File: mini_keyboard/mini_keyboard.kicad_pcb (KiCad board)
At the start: 2 copper layers, 4 parts, among them U1 MX1A-11NN, U2 MX1A-11NN, U3 MX1A-11NN, U4 MX1A-11NN

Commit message: adding more keys and looking at spacing
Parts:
- added U10: MX1A-11NN, pedrolib:CHERRY_MX1A-11NN_SWITCH, F.Cu at (54.0, 25.4)
- added U11: MX1A-11NN, pedrolib:CHERRY_MX1A-11NN_SWITCH, F.Cu at (73.0, 25.4)
- added U12: MX1A-11NN, pedrolib:CHERRY_MX1A-11NN_SWITCH, F.Cu at (92.1, 25.4)
- added U5: MX1A-11NN, pedrolib:CHERRY_MX1A-11NN_SWITCH, F.Cu at (44.5, 44.5)
- added U6: MX1A-11NN, pedrolib:CHERRY_MX1A-11NN_SWITCH, F.Cu at (63.5, 44.5)
- added U7: MX1A-11NN, pedrolib:CHERRY_MX1A-11NN_SWITCH, F.Cu at (82.5, 44.5)
- added U8: MX1A-11NN, pedrolib:CHERRY_MX1A-11NN_SWITCH, F.Cu at (101.6, 44.5)
- added U9: MX1A-11NN, pedrolib:CHERRY_MX1A-11NN_SWITCH, F.Cu at (34.9, 25.4)
- moved U4 59.1 mm to (108.0, 63.5)
- moved U1 50.0 mm to (50.8, 63.5)
- moved U3 43.6 mm to (88.9, 63.5)
- moved U2 39.6 mm to (69.8, 63.5)

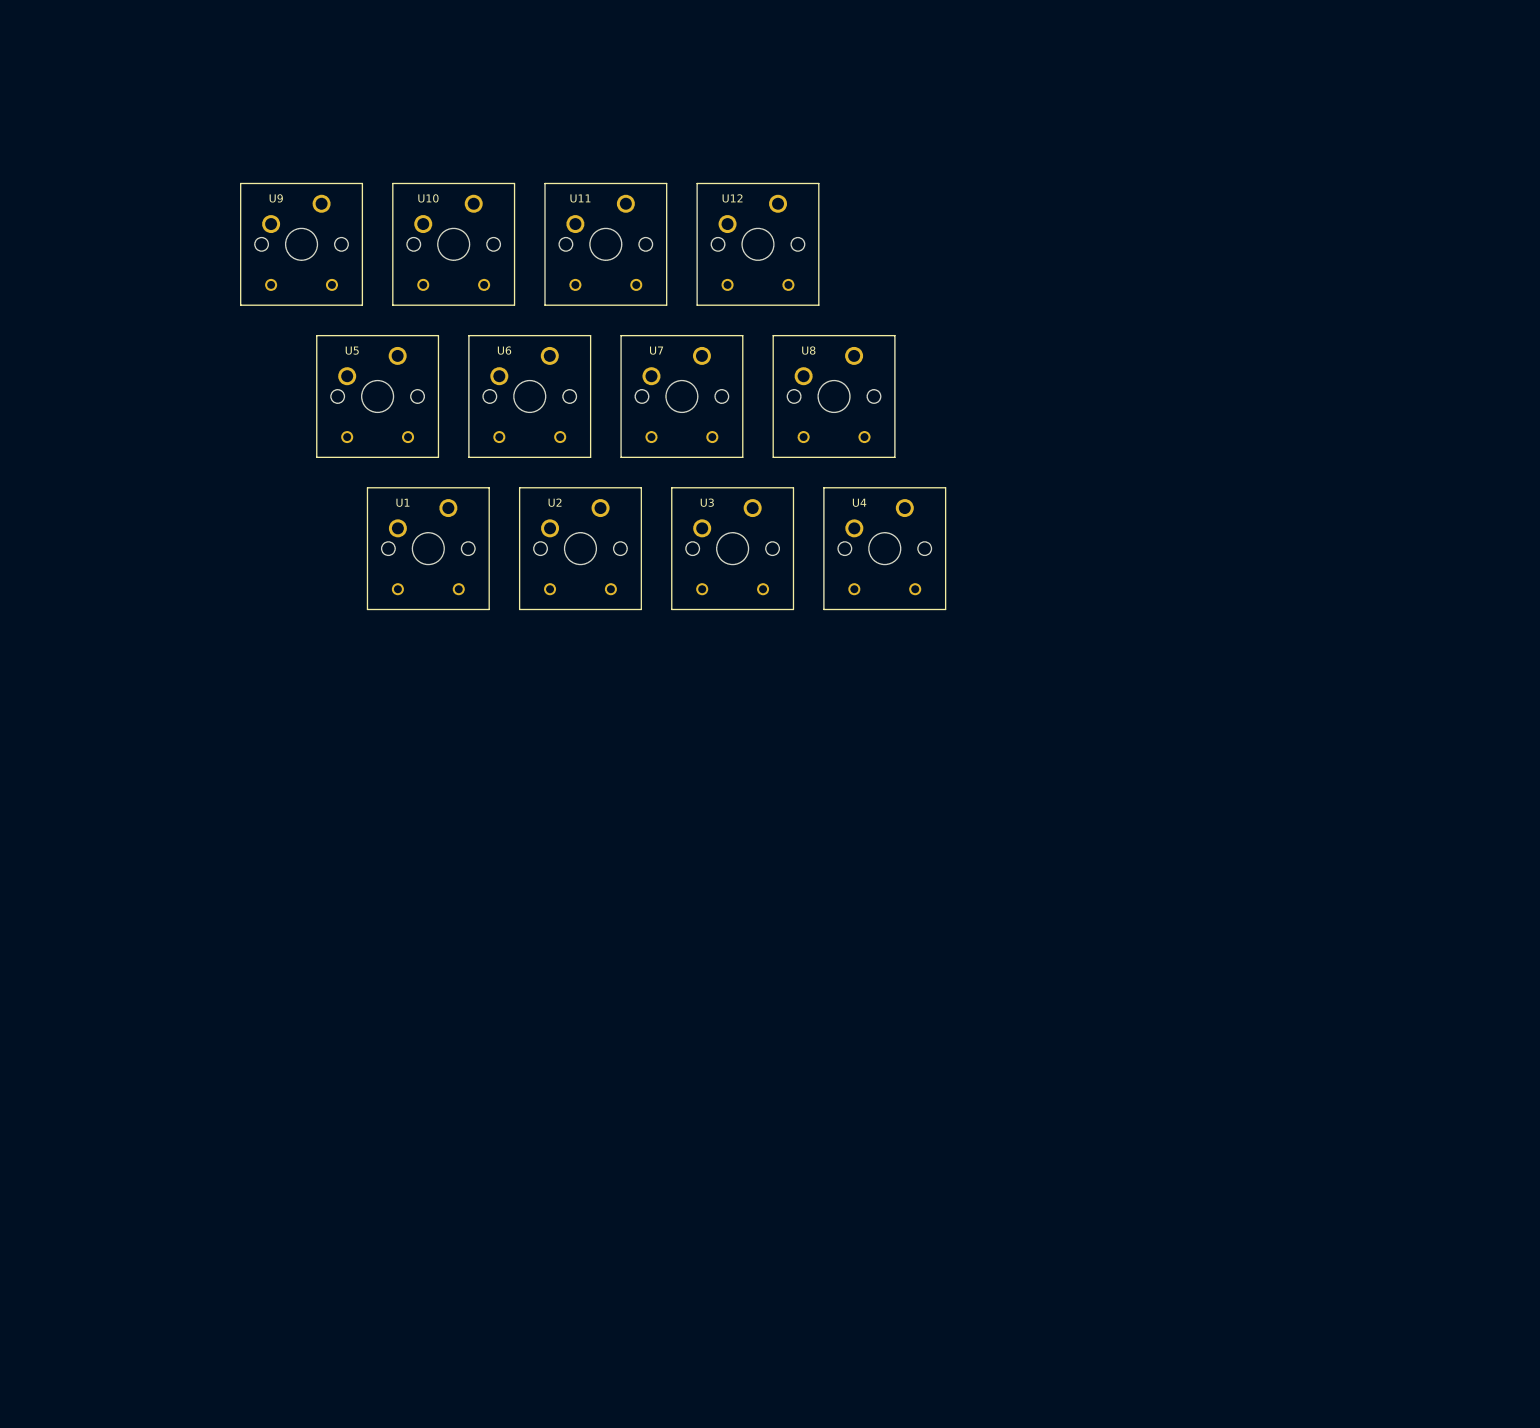
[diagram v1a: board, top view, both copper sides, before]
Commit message: updating library for keyboard work
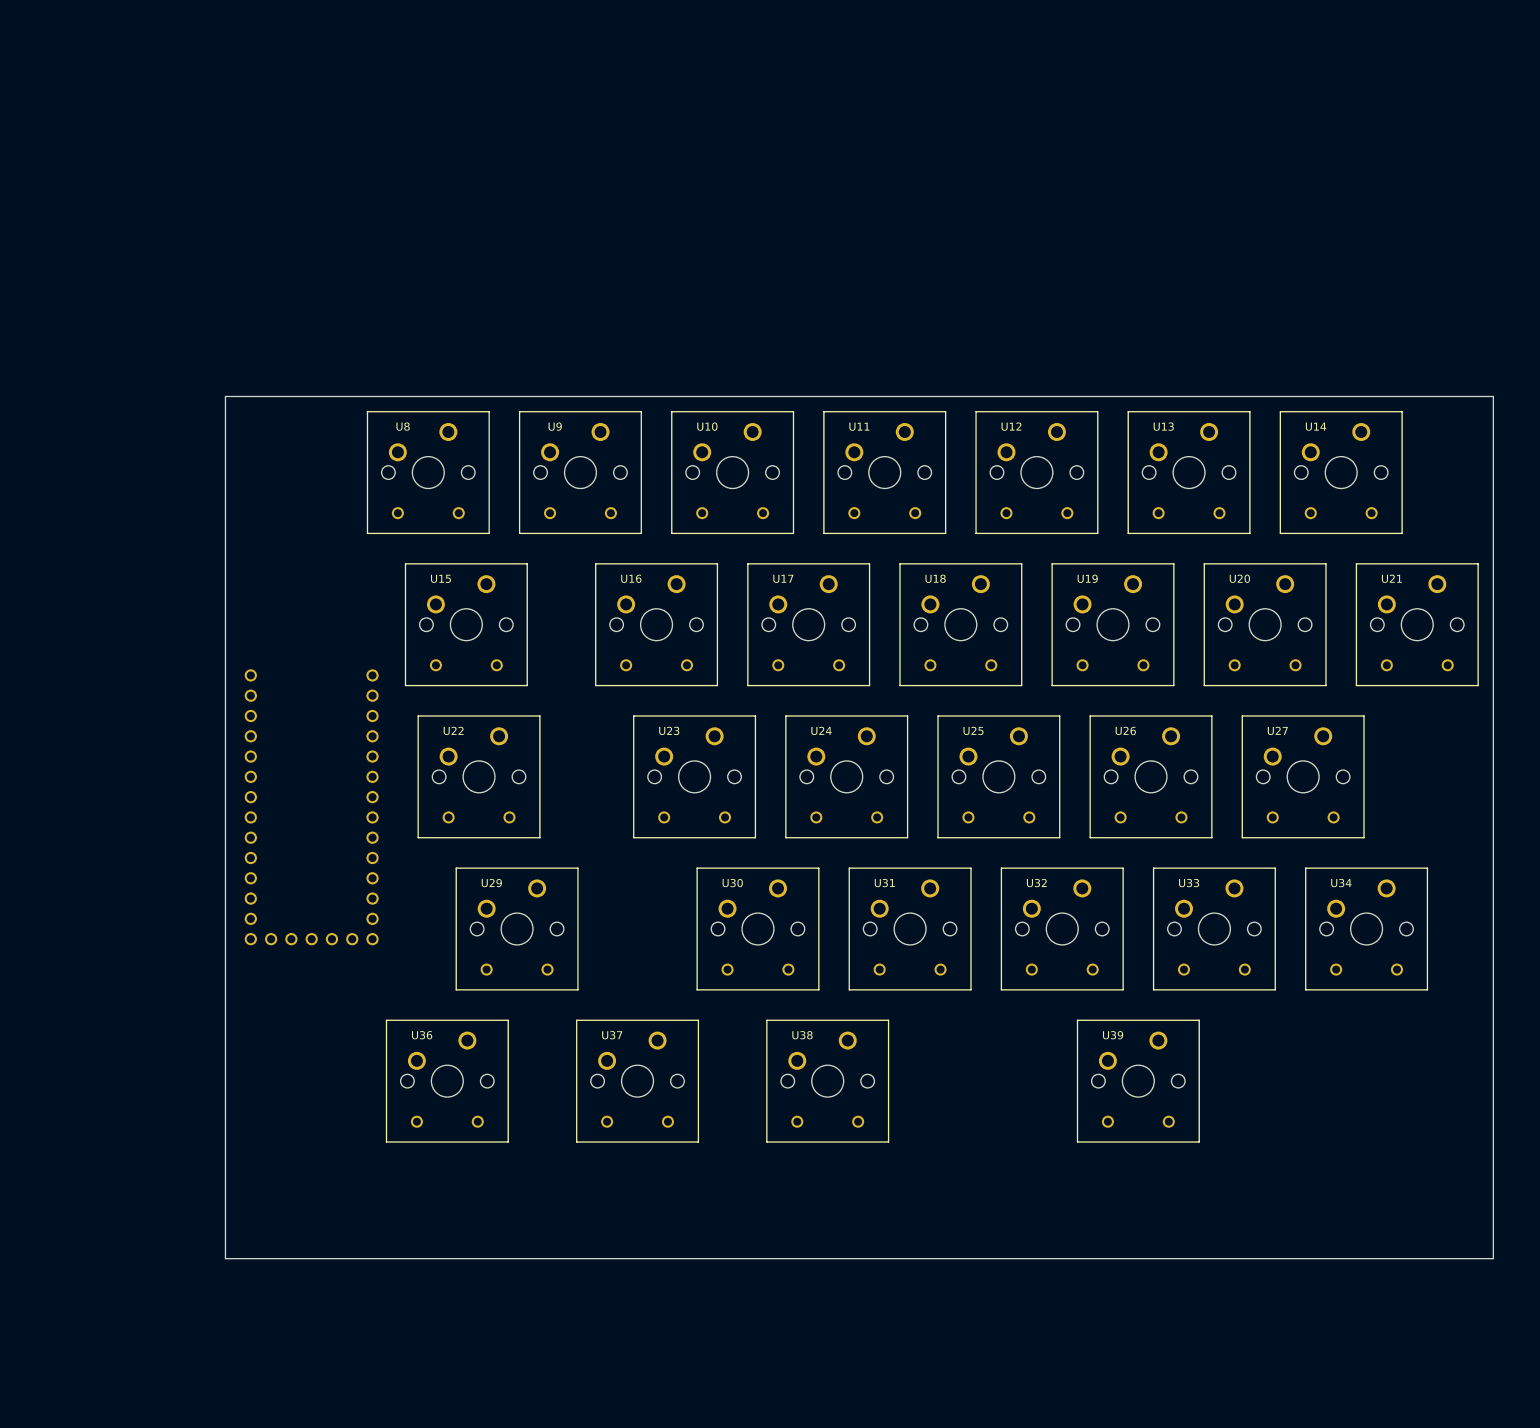
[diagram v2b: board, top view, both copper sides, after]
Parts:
- removed U1, U2, U3, U4, U5, U6, U7: MX1A-11NN, pedrolib:CHERRY_MX1A-11NN_SWITCH
- added U100: DEV-15583, pedrolib:MODULE_DEV-15583, B.Cu at (36.2, 95.9)
- added U13: MX1A-11NN, pedrolib:CHERRY_MX1A-11NN_SWITCH, F.Cu at (146.1, 54.0)
- added U14: MX1A-11NN, pedrolib:CHERRY_MX1A-11NN_SWITCH, F.Cu at (165.1, 54.0)
- added U15: MX1A-11NN, pedrolib:CHERRY_MX1A-11NN_SWITCH, F.Cu at (55.6, 73.0)
- added U16: MX1A-11NN, pedrolib:CHERRY_MX1A-11NN_SWITCH, F.Cu at (79.4, 73.0)
- added U17: MX1A-11NN, pedrolib:CHERRY_MX1A-11NN_SWITCH, F.Cu at (98.4, 73.0)
- added U18: MX1A-11NN, pedrolib:CHERRY_MX1A-11NN_SWITCH, F.Cu at (117.5, 73.0)
- added U19: MX1A-11NN, pedrolib:CHERRY_MX1A-11NN_SWITCH, F.Cu at (136.5, 73.0)
- added U20: MX1A-11NN, pedrolib:CHERRY_MX1A-11NN_SWITCH, F.Cu at (155.6, 73.0)
- added U21: MX1A-11NN, pedrolib:CHERRY_MX1A-11NN_SWITCH, F.Cu at (174.6, 73.0)
- added U22: MX1A-11NN, pedrolib:CHERRY_MX1A-11NN_SWITCH, F.Cu at (57.1, 92.1)
- added U23: MX1A-11NN, pedrolib:CHERRY_MX1A-11NN_SWITCH, F.Cu at (84.1, 92.1)
- added U24: MX1A-11NN, pedrolib:CHERRY_MX1A-11NN_SWITCH, F.Cu at (103.2, 92.1)
- added U25: MX1A-11NN, pedrolib:CHERRY_MX1A-11NN_SWITCH, F.Cu at (122.2, 92.1)
- added U26: MX1A-11NN, pedrolib:CHERRY_MX1A-11NN_SWITCH, F.Cu at (141.3, 92.1)
- added U27: MX1A-11NN, pedrolib:CHERRY_MX1A-11NN_SWITCH, F.Cu at (160.3, 92.1)
- added U29: MX1A-11NN, pedrolib:CHERRY_MX1A-11NN_SWITCH, F.Cu at (61.9, 111.1)
- added U30: MX1A-11NN, pedrolib:CHERRY_MX1A-11NN_SWITCH, F.Cu at (92.1, 111.1)
- added U31: MX1A-11NN, pedrolib:CHERRY_MX1A-11NN_SWITCH, F.Cu at (111.1, 111.1)
- added U32: MX1A-11NN, pedrolib:CHERRY_MX1A-11NN_SWITCH, F.Cu at (130.2, 111.1)
- added U33: MX1A-11NN, pedrolib:CHERRY_MX1A-11NN_SWITCH, F.Cu at (149.2, 111.1)
- added U34: MX1A-11NN, pedrolib:CHERRY_MX1A-11NN_SWITCH, F.Cu at (168.3, 111.1)
- added U36: MX1A-11NN, pedrolib:CHERRY_MX1A-11NN_SWITCH, F.Cu at (53.2, 130.2)
- added U37: MX1A-11NN, pedrolib:CHERRY_MX1A-11NN_SWITCH, F.Cu at (77.0, 130.2)
- added U38: MX1A-11NN, pedrolib:CHERRY_MX1A-11NN_SWITCH, F.Cu at (100.8, 130.2)
- added U39: MX1A-11NN, pedrolib:CHERRY_MX1A-11NN_SWITCH, F.Cu at (139.7, 130.2)
- moved U8 51.7 mm to (50.8, 54.0)
- moved U10 45.1 mm to (88.9, 54.0)
- moved U11 45.1 mm to (108.0, 54.0)
- moved U12 45.1 mm to (127.0, 54.0)
- moved U9 45.1 mm to (69.8, 54.0)
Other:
- board outline added: 158.8 x 108 mm

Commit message: library update for keyboard
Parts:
- moved U100 9.55 mm to (36.8, 86.4)

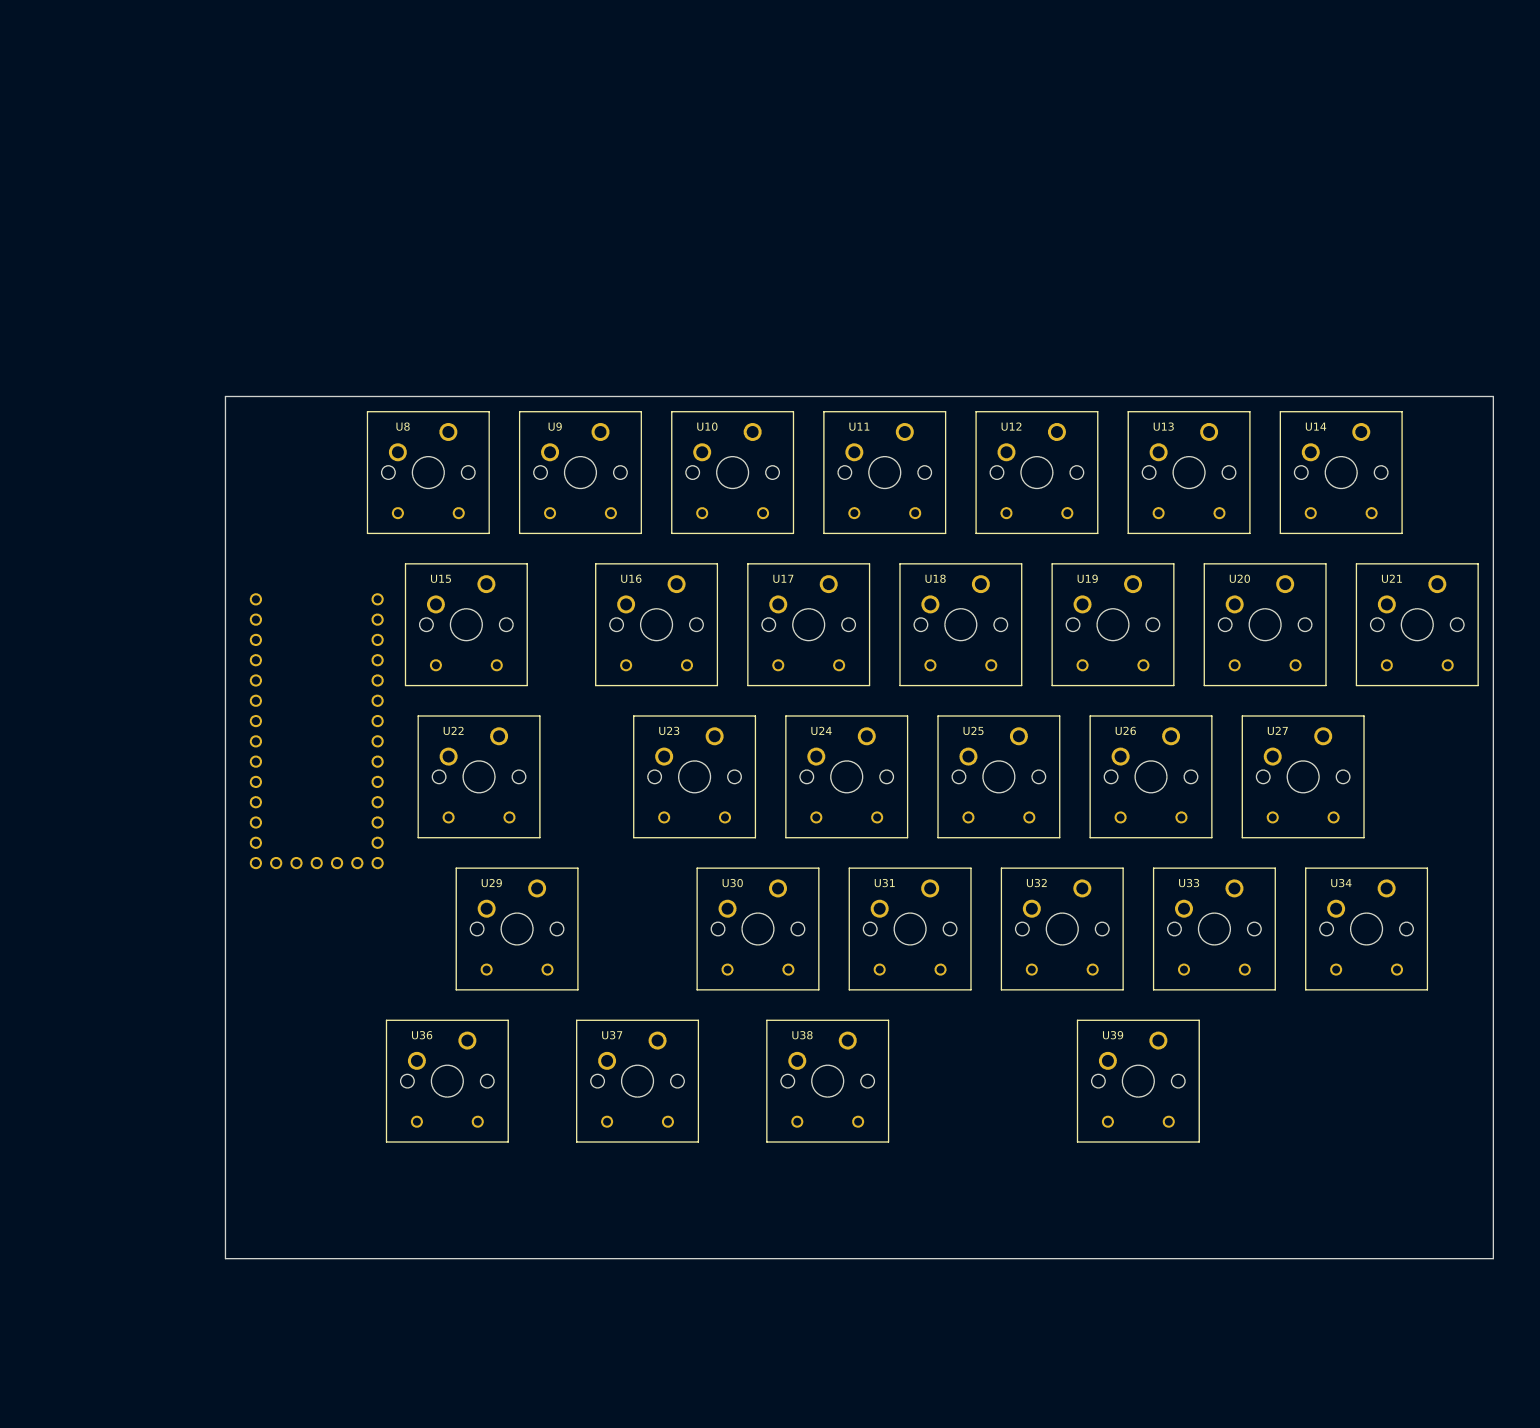
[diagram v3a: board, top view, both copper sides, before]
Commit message: added Teensy 4.0
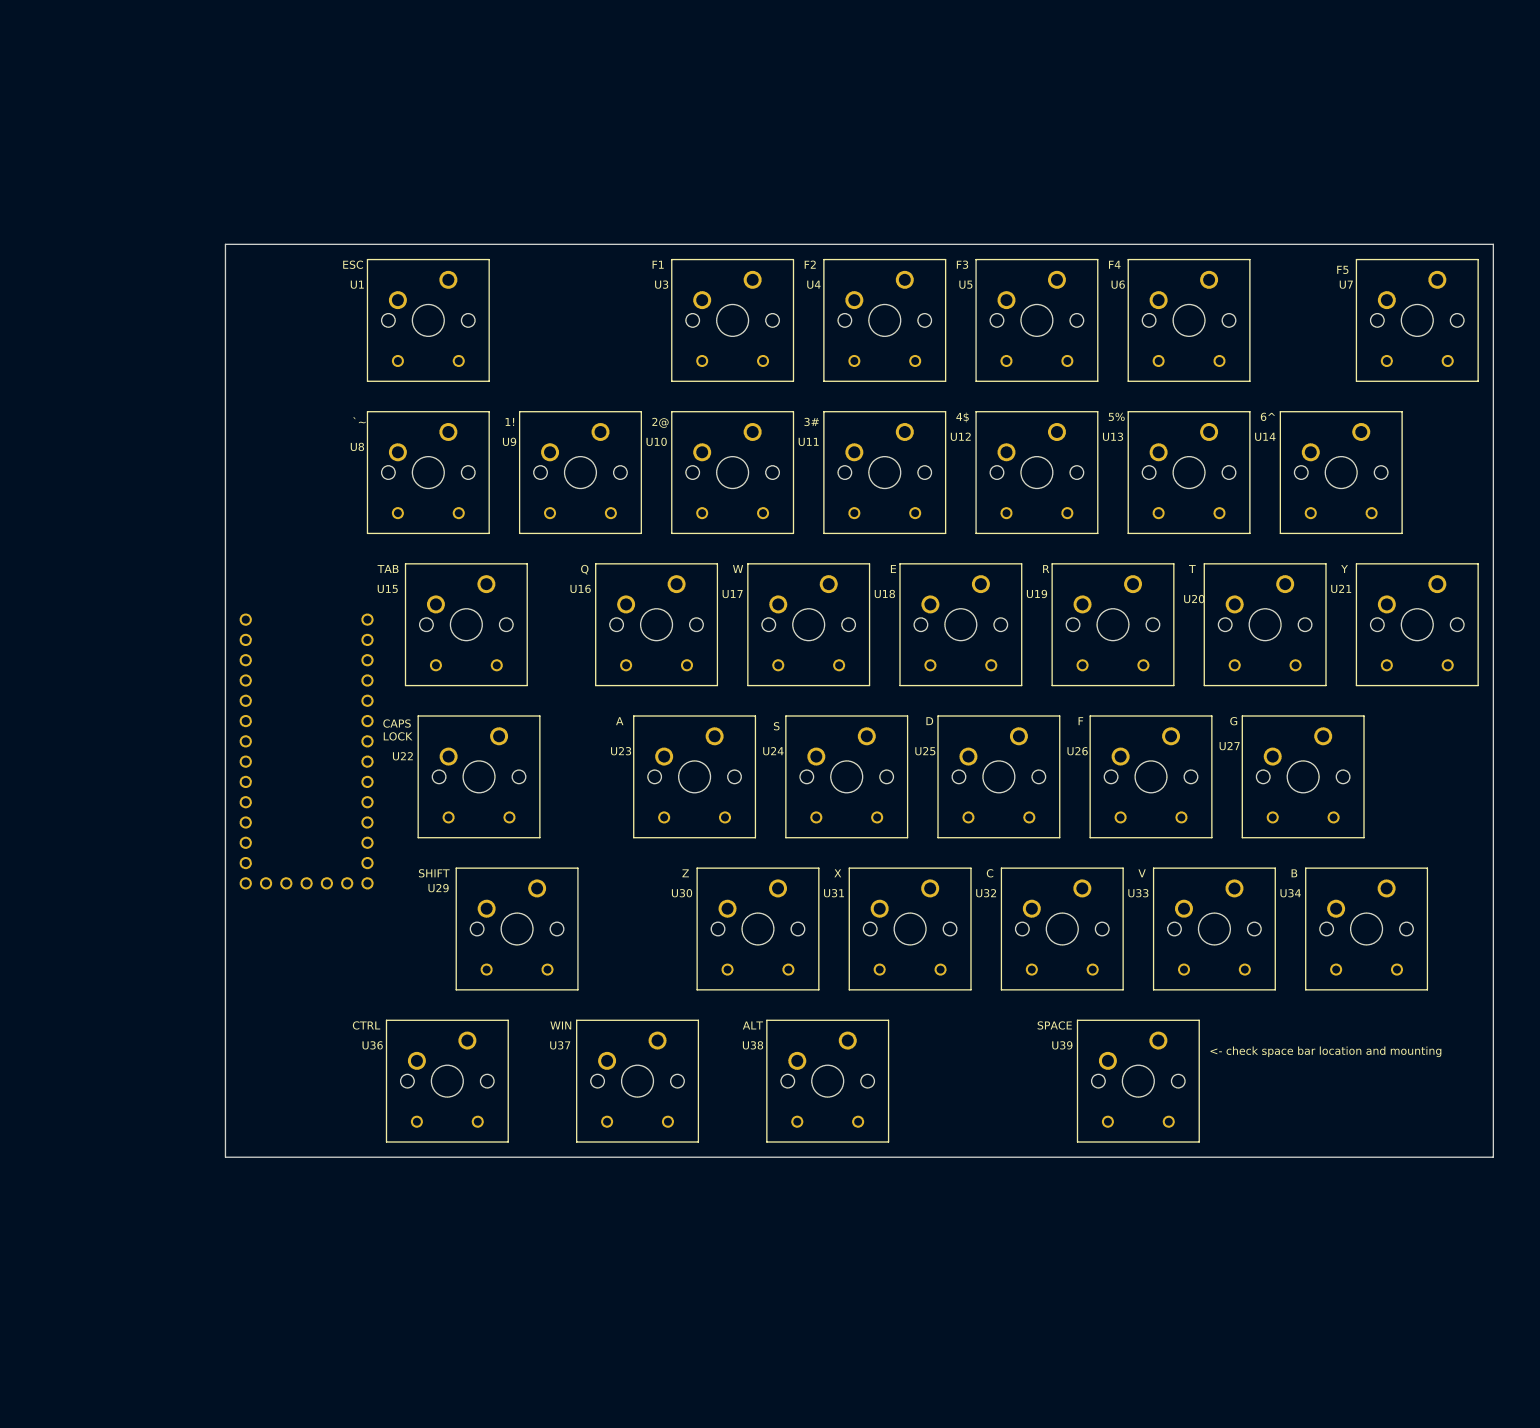
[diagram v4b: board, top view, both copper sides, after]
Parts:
- added U1: MX1A-11NN, pedrolib:CHERRY_MX1A-11NN_SWITCH, F.Cu at (50.8, 34.9)
- added U3: MX1A-11NN, pedrolib:CHERRY_MX1A-11NN_SWITCH, F.Cu at (88.9, 34.9)
- added U4: MX1A-11NN, pedrolib:CHERRY_MX1A-11NN_SWITCH, F.Cu at (108.0, 34.9)
- added U5: MX1A-11NN, pedrolib:CHERRY_MX1A-11NN_SWITCH, F.Cu at (127.0, 34.9)
- added U6: MX1A-11NN, pedrolib:CHERRY_MX1A-11NN_SWITCH, F.Cu at (146.1, 34.9)
- added U7: MX1A-11NN, pedrolib:CHERRY_MX1A-11NN_SWITCH, F.Cu at (174.6, 34.9)
- moved U100 2.84 mm to (35.6, 88.9)
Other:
- board size 158.8 x 108 mm -> 158.8 x 114.3 mm
- board text added: "1!"
- board text added: "2@"
- board text added: "3#"
- board text added: "4$"
- board text added: "5%"
- board text added: "6^"
- board text added: "<- check space bar location and mounting"
- board text added: "A"
- board text added: "ALT"
- board text added: "B"
- board text added: "C"
- board text added: "CAPS LOCK"
- board text added: "CTRL"
- board text added: "D"
- board text added: "E"
- board text added: "ESC"
- board text added: "F"
- board text added: "F1"
- board text added: "F2"
- board text added: "F3"
- board text added: "F4"
- board text added: "F5"
- board text added: "G"
- board text added: "Q"
- board text added: "R"
- board text added: "S"
- board text added: "SHIFT"
- board text added: "SPACE"
- board text added: "T"
- board text added: "TAB"
- board text added: "V"
- board text added: "W"
- board text added: "WIN"
- board text added: "X"
- board text added: "Y"
- board text added: "Z"
- board text added: "`~"
